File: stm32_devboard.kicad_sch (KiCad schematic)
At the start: 1 part, among them U1 STM32F072CBTx

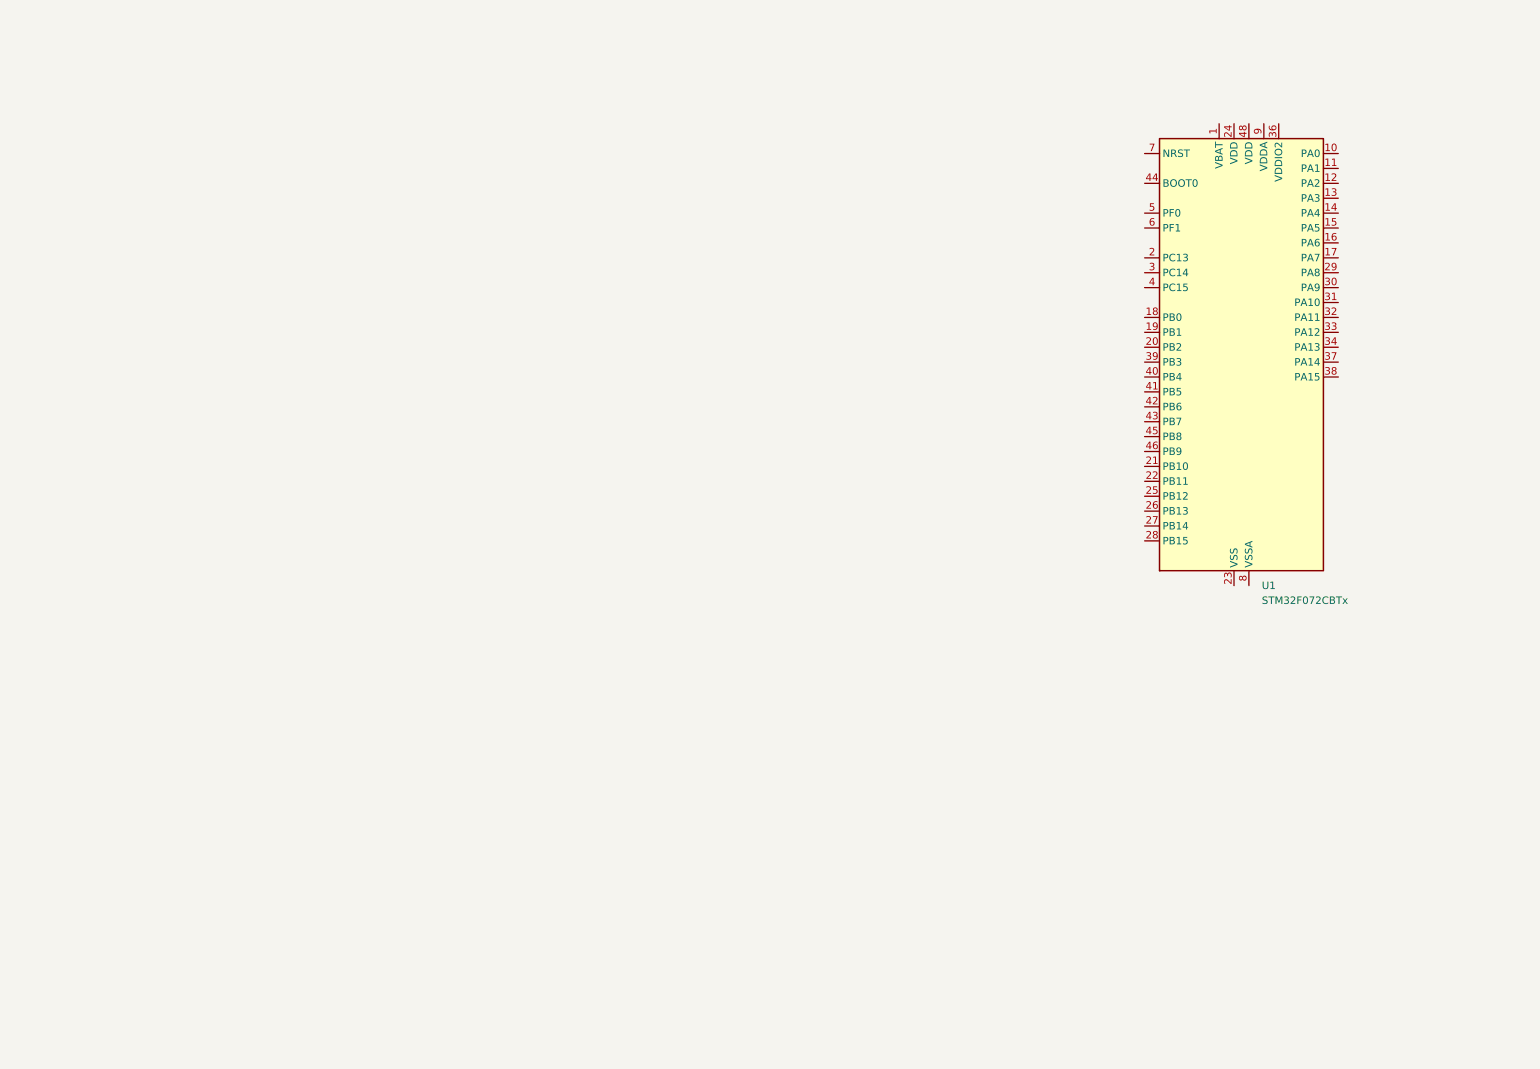
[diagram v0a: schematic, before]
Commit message: schematic done: errors not yet corrected
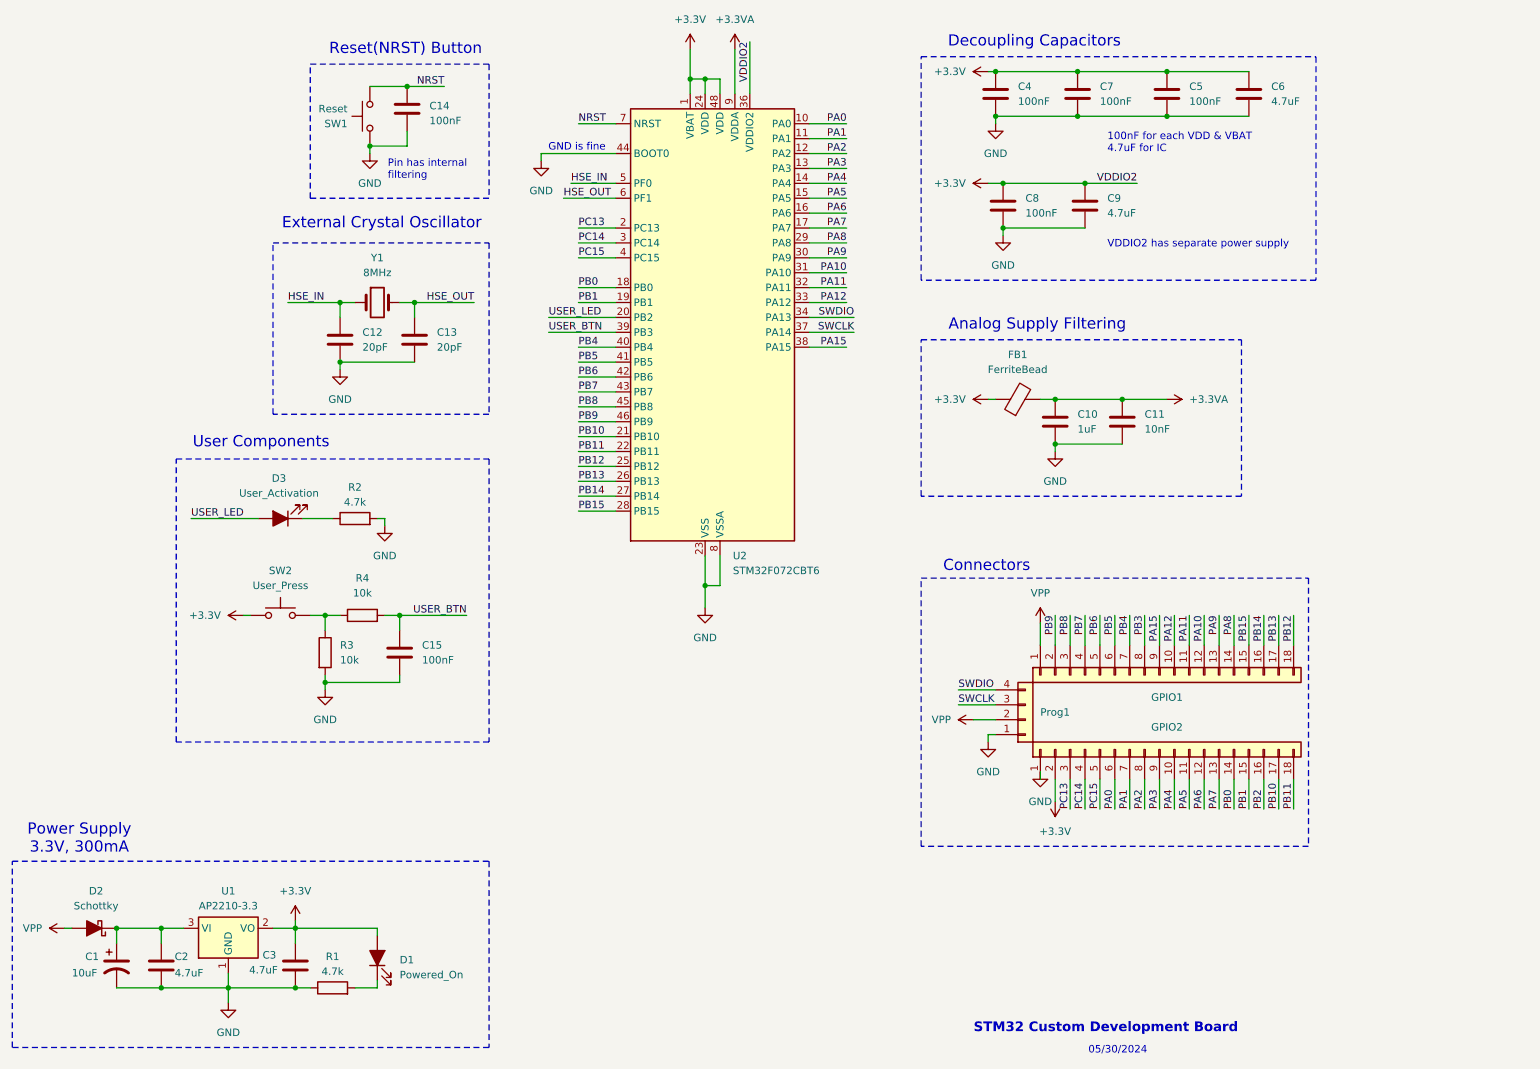
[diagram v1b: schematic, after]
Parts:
- added C1: 10uF, symbol Device:C_Polarized_US
- added C10: 1uF, symbol Device:C
- added C11: 10nF, symbol Device:C
- added C12, C13: 20pF, symbol Device:C
- added C14, C15, C4, C5, C7, C8: 100nF, symbol Device:C
- added C2, C3, C6, C9: 4.7uF, symbol Device:C
- added D1: Powered_On, symbol Device:LED_Filled
- added D2: Schottky, symbol Device:D_Schottky_Filled
- added D3: User_Activation, symbol Device:LED_Filled
- added FB1: FerriteBead, symbol Device:FerriteBead
- added GPIO1, GPIO2: Conn_01x18, symbol Connector_Generic:Conn_01x18
- added Prog1: Conn_01x04, symbol Connector_Generic:Conn_01x04
- added R1, R2: 4.7k, symbol Device:R
- added R3, R4: 10k, symbol Device:R
- added SW1: Reset, symbol Switch:SW_Push
- added SW2: User_Press, symbol Switch:SW_Push
- added U1: AP2210-3.3, Package_TO_SOT_SMD:SOT-223-3_TabPin2, symbol Regulator_Linear:AP1117-33
- added Y1: 8MHz, symbol Device:Crystal
- U2: renamed from U1; value STM32F072CBTx -> STM32F072CBT6
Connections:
- net +3.3V: now reaches U2.1 (VBAT)
- net +3.3V: now also U2.24 (VDD), U2.36 (VDDIO2), U2.48 (VDD), C3.1, C4.1, C5.1, C6.1, C7.1, C8.1, C9.1, D1.2 (A), FB1.1, GPIO2.2 (Pin_2), SW2.1, U1.2 (VO)
- net PA0: now reaches U2.10 (PA0)
- net PA0: now also GPIO2.6 (Pin_6)
- net PA1: now reaches U2.11 (PA1)
- net PA1: now also GPIO2.7 (Pin_7)
- net PA2: now reaches U2.12 (PA2)
- net PA2: now also GPIO2.8 (Pin_8)
- net PA3: now reaches U2.13 (PA3)
- net PA3: now also GPIO2.9 (Pin_9)
- net PA4: now reaches U2.14 (PA4)
- net PA4: now also GPIO2.10 (Pin_10)
- net PA5: now reaches U2.15 (PA5)
- net PA5: now also GPIO2.11 (Pin_11)
- net PA6: now reaches U2.16 (PA6)
- net PA6: now also GPIO2.12 (Pin_12)
- net PA7: now reaches U2.17 (PA7)
- net PA7: now also GPIO2.13 (Pin_13)
- net PB0: now reaches U2.18 (PB0)
- net PB0: now also GPIO2.14 (Pin_14)
- net PB1: now reaches U2.19 (PB1)
- net PB1: now also GPIO2.15 (Pin_15)
- net PC13: now reaches U2.2 (PC13)
- net PC13: now also GPIO2.3 (Pin_3)
- net USER_LED: now reaches U2.20 (PB2)
- net USER_LED: now also D3.2 (A)
- net PB10: now reaches U2.21 (PB10)
- net PB10: now also GPIO2.17 (Pin_17)
- net PB11: now reaches U2.22 (PB11)
- net PB11: now also GPIO2.18 (Pin_18)
- net GND: now reaches U2.23 (VSS), U2.35 (VSS), U2.47 (VSS)
- net GND: now also U2.44 (BOOT0), U2.8 (VSSA), C1.2, C10.2, C11.2, C12.2, C13.2, C14.2, C15.2, C2.2, C3.2, C4.2, C5.2, C6.2, C7.2, C8.2, C9.2, GPIO2.1 (Pin_1), Prog1.1 (Pin_1), R1.1, R2.2, R3.2, SW1.1, U1.1 (GND)
- net PB12: now reaches U2.25 (PB12)
- net PB12: now also GPIO1.18 (Pin_18)
- net PB13: now reaches U2.26 (PB13)
- net PB13: now also GPIO1.17 (Pin_17)
- net PB14: now reaches U2.27 (PB14)
- net PB14: now also GPIO1.16 (Pin_16)
- net PB15: now reaches U2.28 (PB15)
- net PB15: now also GPIO1.15 (Pin_15)
- net PA8: now reaches U2.29 (PA8)
- net PA8: now also GPIO1.14 (Pin_14)
- net PC14: now reaches U2.3 (PC14)
- net PC14: now also GPIO2.4 (Pin_4)
- net PA9: now reaches U2.30 (PA9)
- net PA9: now also GPIO1.13 (Pin_13)
- net PA10: now reaches U2.31 (PA10)
- net PA10: now also GPIO1.12 (Pin_12)
- net PA11: now reaches U2.32 (PA11)
- net PA11: now also GPIO1.11 (Pin_11)
- net PA12: now reaches U2.33 (PA12)
- net PA12: now also GPIO1.10 (Pin_10)
- net SWDIO: now reaches U2.34 (PA13)
- net SWDIO: now also Prog1.4 (Pin_4)
- net SWCLK: now reaches U2.37 (PA14)
- net SWCLK: now also Prog1.3 (Pin_3)
- net PA15: now reaches U2.38 (PA15)
- net PA15: now also GPIO1.9 (Pin_9)
- net USER_BTN: now reaches U2.39 (PB3)
- net USER_BTN: now also C15.1, R4.2
- net PC15: now reaches U2.4 (PC15)
- net PC15: now also GPIO2.5 (Pin_5)
- net PB4: now reaches U2.40 (PB4)
- net PB4: now also GPIO1.7 (Pin_7)
- net PB5: now reaches U2.41 (PB5)
- net PB5: now also GPIO1.6 (Pin_6)
- net PB6: now reaches U2.42 (PB6)
- net PB6: now also GPIO1.5 (Pin_5)
- net PB7: now reaches U2.43 (PB7)
- net PB7: now also GPIO1.4 (Pin_4)
- net PB8: now reaches U2.45 (PB8)
- net PB8: now also GPIO1.3 (Pin_3)
- net PB9: now reaches U2.46 (PB9)
- net PB9: now also GPIO1.2 (Pin_2)
- net HSE_IN: now reaches U2.5 (PF0)
- net HSE_IN: now also C12.1, Y1.1
- net HSE_OUT: now reaches U2.6 (PF1)
- net HSE_OUT: now also C13.1, Y1.2
- net NRST: now reaches U2.7 (NRST)
- net NRST: now also C14.1, SW1.2
- net +3.3VA: now reaches U2.9 (VDDA)
- net +3.3VA: now also C10.1, C11.1, FB1.2
- new net: R3.1, R4.1, SW2.2
- new net: D3.1 (K), R2.1
- new net: D1.1 (K), R1.2
- new net: C1.1, C2.1, D2.1 (K), U1.3 (VI)
- new net PB2: GPIO2.16 (Pin_16)
- new net PB3: GPIO1.8 (Pin_8)
- new net VPP: D2.2 (A), GPIO1.1 (Pin_1), Prog1.2 (Pin_2)
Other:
- note added: "05/30/2024"
- note added: "100nF for each VDD & VBAT 4.7uF for IC"
- note added: "Analog Supply Filtering"
- note added: "Connectors"
- note added: "Decoupling Capacitors"
- note added: "External Crystal Oscillator"
- note added: "GND is fine"
- note added: "Pin has internal filtering"
- note added: "Power Supply 3.3V, 300mA"
- note added: "Reset(NRST) Button"
- note added: "STM32 Custom Development Board"
- note added: "User Components"
- note added: "VDDIO2 has separate power supply"
- moved on the sheet: U2

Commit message: Schematic Rev. 2: Fix all errors, finalized version for PCB
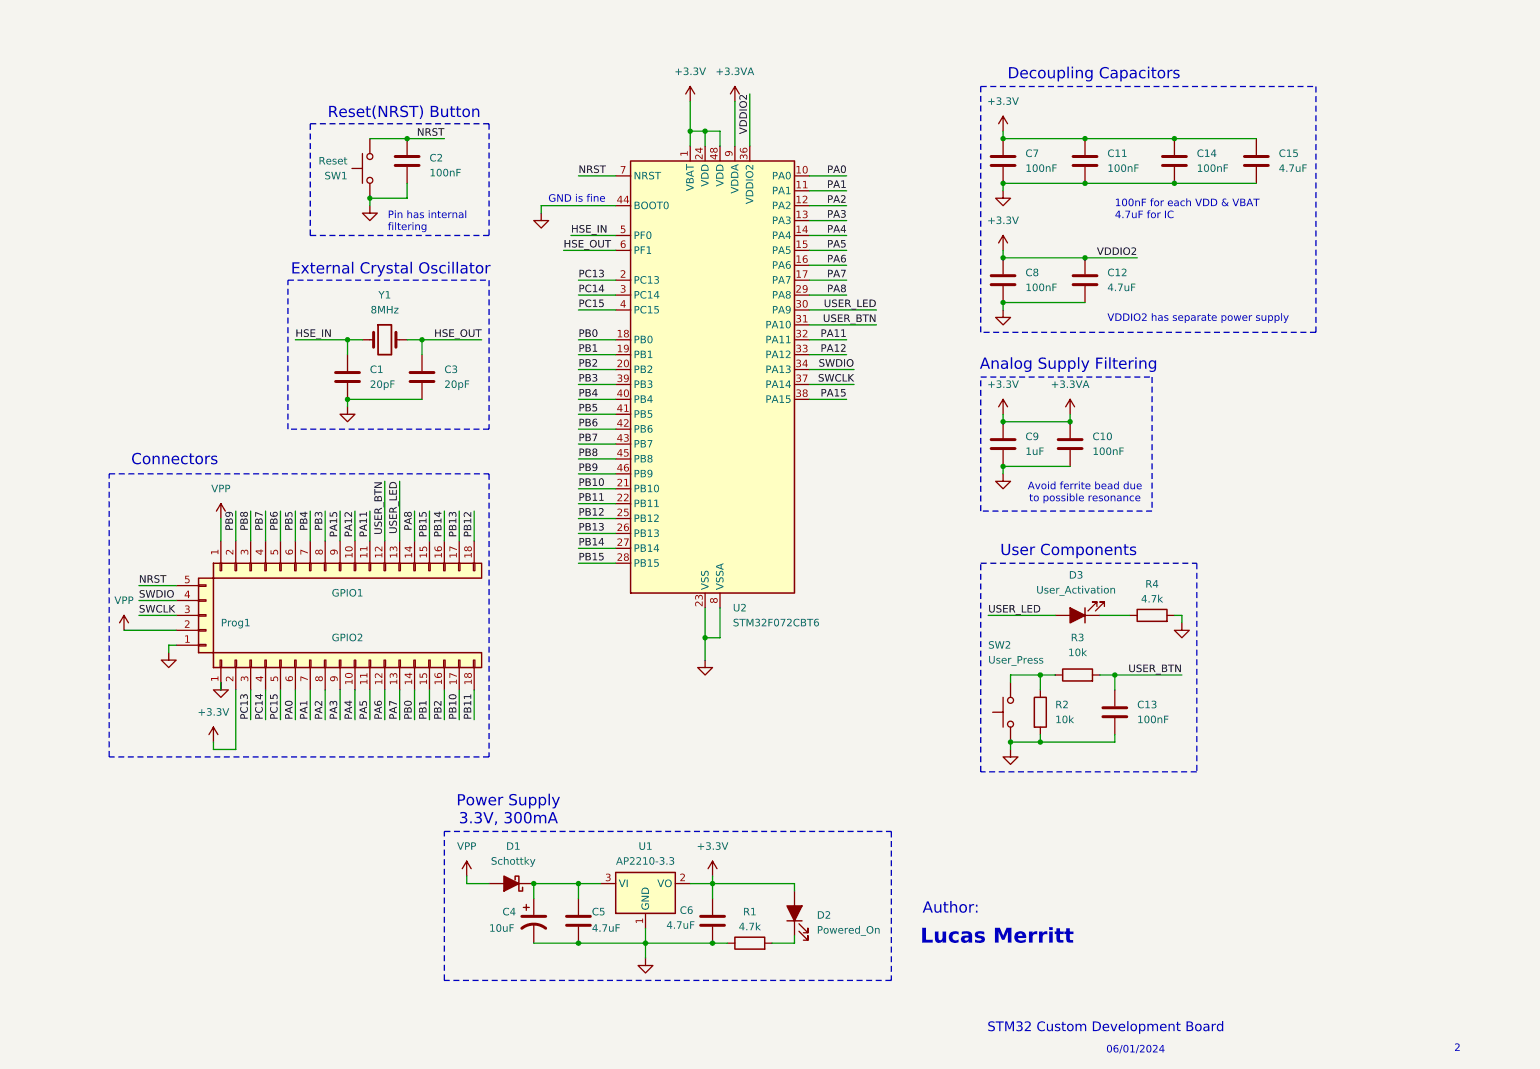
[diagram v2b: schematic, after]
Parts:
- removed FB1: FerriteBead, symbol Device:FerriteBead
- removed Prog1: Conn_01x04, symbol Connector_Generic:Conn_01x04
- added Prog1: Conn_01x05, symbol Connector_Generic:Conn_01x05
- C10: renamed from C11; value 10nF -> 100nF
- renumbered C12 to C1, C7 to C11, C9 to C12, C15 to C13, C5 to C14, C6 to C15, C14 to C2, C13 to C3, C1 to C4, C2 to C5, C3 to C6, C4 to C7, C10 to C9, D2 to D1, D1 to D2, R3 to R2, R4 to R3, R2 to R4
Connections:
- net +3.3VA is gone; now on net +3.3V: C10.1, C9.1, U2.9 (VDDA)
- net PA10 is gone; now on net USER_BTN: GPIO1.12 (Pin_12), U2.31 (PA10)
- net PA9 is gone; now on net USER_LED: GPIO1.13 (Pin_13), U2.30 (PA9)
- net +3.3V: no longer SW2.1
- net GND: now also SW2.1, Prog1.1 (Pin_1)
- net NRST: now also Prog1.5 (Pin_5)
- net PB2: now also U2.20 (PB2)
- net PB3: now also U2.39 (PB3)
- net SWCLK: now also Prog1.3 (Pin_3)
- net SWDIO: now also Prog1.4 (Pin_4)
- net USER_BTN: no longer U2.39 (PB3)
- net USER_LED: no longer U2.20 (PB2)
- net VPP: now also Prog1.2 (Pin_2)
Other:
- note added: "06/01/2024"
- note added: "2"
- note added: "Author:"
- note added: "Avoid ferrite bead due to possible resonance"
- note added: "Lucas Merritt"
- note removed: "05/30/2024"
- moved on the sheet: C1, C10, C11, C12, C13, C14, C15, C2, C3, C4, C5, C6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

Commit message: PCB/schematic updates
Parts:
- C1, C3: footprint (none) -> Capacitor_SMD:C_0805_2012Metric
- C10, C11, C12, C13, C14, C15, C2, C5, C6, C7, C8, C9: footprint (none) -> Capacitor_SMD:C_0402_1005Metric
- C4: footprint (none) -> Capacitor_Tantalum_SMD:CP_EIA-3216-18_Kemet-A
- D1: footprint (none) -> Diode_SMD:D_SOD-123
- D2: footprint (none) -> LED_SMD:LED_0603_1608Metric
- D3: footprint (none) -> LED_SMD:LED_0805_2012Metric
- GPIO1, GPIO2: footprint (none) -> Connector_PinHeader_2.54mm:PinHeader_1x18_P2.54mm_Vertical
- Prog1: footprint (none) -> Connector_PinHeader_2.54mm:PinHeader_1x05_P2.54mm_Horizontal
- R1, R4: footprint (none) -> Resistor_SMD:R_0805_2012Metric
- R2, R3: footprint (none) -> Resistor_SMD:R_0402_1005Metric
- SW1, SW2: footprint (none) -> Button_Switch_SMD:SW_Push_1P1T_NO_6x6mm_H9.5mm
- U1: value AP2210-3.3 -> XC6206P332MR-G; footprint Package_TO_SOT_SMD:SOT-223-3_TabPin2 -> Package_TO_SOT_SMD:SOT-23-3
- Y1: footprint (none) -> Crystal:Crystal_SMD_HC49-SD
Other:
- note added: "3 footprints"
- note added: "Power Supply 3.3V, 200mA"
- note removed: "2"
- note removed: "Power Supply 3.3V, 300mA"
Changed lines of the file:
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@@
 		)
 	)
-	(text "Power Supply\n3.3V, 300mA"
+	(text "Power Supply\n3.3V, 200mA"
 		(exclude_from_sim no)
 		(at 108.712 152.654 0)
@@
 		)
 	)
-	(text "2"
+	(text "3 footprints"
 		(exclude_from_sim no)
-		(at 270.51 193.294 0)
+		(at 275.082 193.548 0)
 		(effects
 			(font
@@
 			)
 		)
-		(property "Footprint" ""
+		(property "Footprint" "Resistor_SMD:R_0402_1005Metric"
 			(at 197.612 135.89 90)
 			(effects
@@
 			)
 		)
-		(property "Footprint" ""
+		(property "Footprint" "Connector_PinHeader_2.54mm:PinHeader_1x18_P2.54mm_Vertical"
 			(at 80.01 127 0)
 			(effects
@@
 			)
 		)
-		(property "Footprint" ""
+		(property "Footprint" "Capacitor_SMD:C_0402_1005Metric"
 			(at 194.0052 45.72 0)
 			(effects
@@
 			)
 		)
-		(property "Footprint" ""
+		(property "Footprint" "Capacitor_SMD:C_0402_1005Metric"
 			(at 205.4352 93.98 0)
 			(effects
@@
 			)
 		)
-		(property "Footprint" ""
+		(property "Footprint" "Capacitor_SMD:C_0402_1005Metric"
 			(at 194.0052 93.98 0)
 			(effects
@@
 			)
 		)
-		(property "Footprint" ""
+		(property "Footprint" "Capacitor_SMD:C_0402_1005Metric"
 			(at 223.2152 45.72 0)
 			(effects
@@
 			)
 		)
-		(property "Footprint" ""
+		(property "Footprint" "Resistor_SMD:R_0402_1005Metric"
 			(at 205.74 131.318 90)
 			(effects
@@
 			)
 		)
-		(property "Footprint" ""
+		(property "Footprint" "Resistor_SMD:R_0805_2012Metric"
 			(at 218.44 121.158 90)
 			(effects
@@
 			)
 		)
-		(property "Footprint" ""
+		(property "Footprint" "Capacitor_SMD:C_0402_1005Metric"
 			(at 237.1852 45.72 0)
 			(effects
@@
 			)
 		)
-		(property "Footprint" ""
+		(property "Footprint" "Resistor_SMD:R_0805_2012Metric"
 			(at 149.86 177.038 90)
 			(effects
@@
 			)
 		)
-		(property "Footprint" ""
+		(property "Footprint" "Diode_SMD:D_SOD-123"
 			(at 109.22 165.1 0)
 			(effects
@@
 			)
 		)
-		(property "Footprint" ""
+		(property "Footprint" "Crystal:Crystal_SMD_HC49-SD"
 			(at 87.63 72.39 0)
 			(effects
@@
 			)
 		)
-		(property "Footprint" ""
+		(property "Footprint" "Button_Switch_SMD:SW_Push_1P1T_NO_6x6mm_H9.5mm"
 			(at 189.23 135.89 0)
 			(effects
@@
 			)
 		)
-		(property "Value" "AP2210-3.3"
+		(property "Value" "XC6206P332MR-G"
 			(at 132.08 161.29 0)
 			(effects
@@
 			)
 		)
-		(property "Footprint" "Package_TO_SOT_SMD:SOT-223-3_TabPin2"
+		(property "Footprint" "Package_TO_SOT_SMD:SOT-23-3"
 			(at 132.08 160.02 0)
 			(effects
@@
 			)
 		)
-		(property "Footprint" ""
+		(property "Footprint" "Capacitor_SMD:C_0402_1005Metric"
 			(at 213.0552 139.7 0)
 			(effects
@@
 			)
 		)
-		(property "Footprint" ""
+		(property "Footprint" "Capacitor_SMD:C_0402_1005Metric"
 			(at 207.9752 66.04 0)
 			(effects
@@
 			)
 		)
-		(property "Footprint" ""
+		(property "Footprint" "Capacitor_SMD:C_0402_1005Metric"
 			(at 92.4052 45.72 0)
 			(effects
@@
 			)
 		)
-		(property "Footprint" ""
+		(property "Footprint" "Connector_PinHeader_2.54mm:PinHeader_1x18_P2.54mm_Vertical"
 			(at 80.01 111.76 0)
 			(effects
@@
 			)
 		)
-		(property "Footprint" ""
+		(property "Footprint" "Capacitor_SMD:C_0402_1005Metric"
 			(at 144.4752 175.26 0)
 			(effects
@@
 			)
 		)
-		(property "Footprint" ""
+		(property "Footprint" "Capacitor_SMD:C_0402_1005Metric"
 			(at 207.9752 45.72 0)
 			(effects
@@
 			)
 		)
-		(property "Footprint" ""
+		(property "Footprint" "LED_SMD:LED_0805_2012Metric"
 			(at 205.74 119.38 0)
 			(effects
@@
 			)
 		)
-		(property "Footprint" ""
+		(property "Footprint" "Capacitor_SMD:C_0805_2012Metric"
 			(at 94.9452 82.55 0)
 			(effects
@@
 			)
 		)
-		(property "Footprint" ""
+		(property "Footprint" "Connector_PinHeader_2.54mm:PinHeader_1x05_P2.54mm_Horizontal"
 			(at 57.15 119.38 0)
 			(effects
@@
 			)
 		)
-		(property "Footprint" ""
+		(property "Footprint" "Capacitor_SMD:C_0402_1005Metric"
 			(at 121.6152 175.26 0)
 			(effects
@@
 			)
 		)
-		(property "Footprint" ""
+		(property "Footprint" "Capacitor_Tantalum_SMD:CP_EIA-3216-18_Kemet-A"
 			(at 113.03 171.45 0)
 			(effects
@@
 			)
 		)
-		(property "Footprint" ""
+		(property "Footprint" "LED_SMD:LED_0603_1608Metric"
 			(at 157.48 170.18 0)
 			(effects
@@
 			)
 		)
-		(property "Footprint" ""
+		(property "Footprint" "Button_Switch_SMD:SW_Push_1P1T_NO_6x6mm_H9.5mm"
 			(at 80.01 43.18 0)
 			(effects
@@
 			)
 		)
-		(property "Footprint" ""
+		(property "Footprint" "Capacitor_SMD:C_0402_1005Metric"
 			(at 194.0052 66.04 0)
 			(effects
@@
 			)
 		)
-		(property "Footprint" ""
+		(property "Footprint" "Capacitor_SMD:C_0805_2012Metric"
 			(at 82.2452 82.55 0)
 			(effects
